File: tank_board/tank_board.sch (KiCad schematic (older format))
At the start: 3 parts

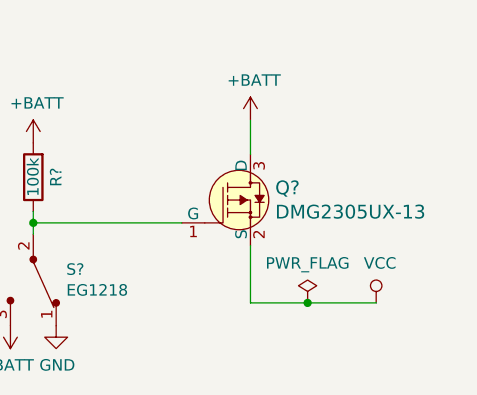
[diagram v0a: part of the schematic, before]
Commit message: Renamed VCC to VBAT
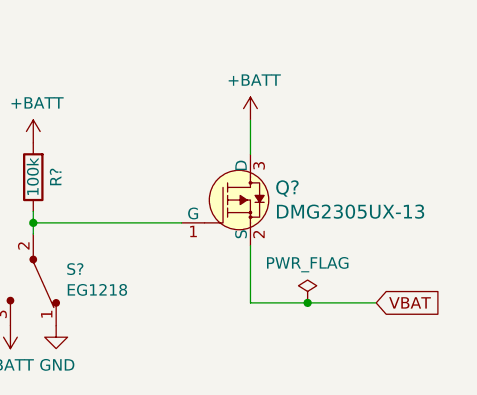
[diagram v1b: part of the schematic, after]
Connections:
- net VCC renamed VBAT
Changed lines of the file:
@@
 	9100 4150 9350 4150
-$Comp
-L power:VCC #PWR?
-U 1 1 5E829323
-P 9650 4150
-F 0 "#PWR?" H 9650 4000 50  0001 C CNN
-F 1 "VCC" H 9667 4323 50  0000 C CNN
-F 2 "" H 9650 4150 50  0001 C CNN
-F 3 "" H 9650 4150 50  0001 C CNN
-	1    9650 4150
-	1    0    0    -1
-$EndComp
 $Comp
 L power:PWR_FLAG #FLG?
@@
 	1    0    0    -1
 $EndComp
+Text GLabel 9650 4150 2    50   Input ~ 0
+VBAT
 $EndSCHEMATC
